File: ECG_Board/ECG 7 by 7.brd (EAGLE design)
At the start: 70 x 70 mm, 7 parts

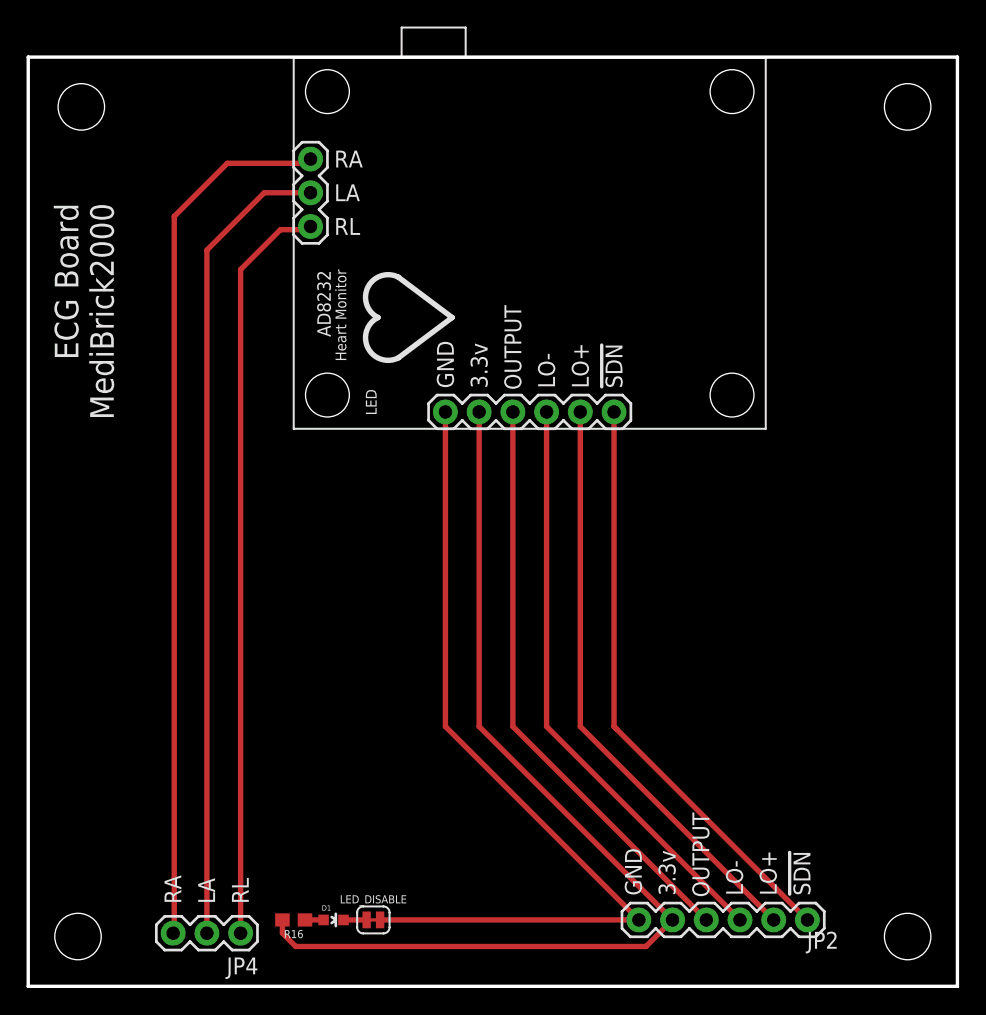
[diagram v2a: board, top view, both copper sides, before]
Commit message: Board Updates
Separated analog and digital ground
Updated routing
Updated silk labeling
Sound board with ES8388 included
Impedance and ECG board
Working on IMU board
Working on Environmental Airquality board
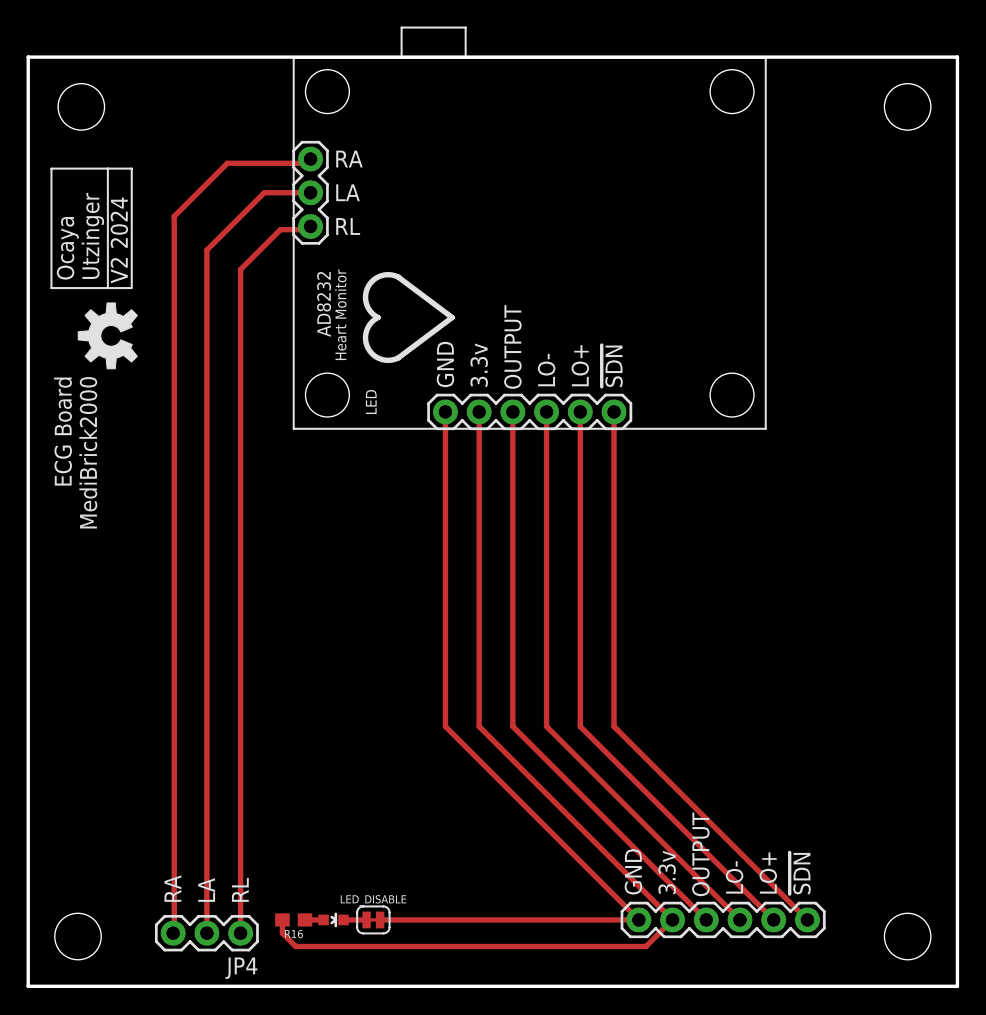
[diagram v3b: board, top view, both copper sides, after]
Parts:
- added U$2: (no value), SparkFun-Aesthetics:OSHW-LOGO-M
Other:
- board text added: "Ocaya Utzinger"
- board text added: "V2 2024"
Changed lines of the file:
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@@
 <text x="10.9" y="6.208" size="1.27" layer="21" font="vector" ratio="15" rot="R90" align="center-left">RA</text>
 <text x="15.98" y="6.208" size="1.27" layer="21" font="vector" ratio="15" rot="R90" align="center-left">RL</text>
-<text x="2" y="59" size="1.778" layer="25" rot="R270">ECG Board
+<text x="2" y="46" size="1.27" layer="25" rot="R270">ECG Board
 MediBrick2000</text>
 <dimension x1="30.5" y1="72" x2="0" y2="72" x3="15.25" y3="75" textsize="1.778" layer="1"/>
+<text x="5.35" y="53.15" size="1.27" layer="25" font="vector" ratio="20" rot="R90">Ocaya
+Utzinger</text>
+<wire x1="1.75" y1="52.6" x2="1.75" y2="61.6" width="0.1524" layer="25"/>
+<wire x1="1.75" y1="61.6" x2="6" y2="61.6" width="0.1524" layer="25"/>
+<wire x1="6" y1="61.6" x2="6" y2="52.6" width="0.1524" layer="25"/>
+<wire x1="6" y1="52.6" x2="1.75" y2="52.6" width="0.1524" layer="25"/>
+<wire x1="7.8" y1="52.65" x2="7.8" y2="61.6" width="0.1524" layer="25"/>
+<wire x1="7.8" y1="52.6" x2="6" y2="52.6" width="0.1524" layer="25"/>
+<wire x1="7.8" y1="61.6" x2="6" y2="61.6" width="0.1524" layer="25"/>
+<text x="7.5" y="52.95" size="1.27" layer="25" font="vector" ratio="20" rot="R90">V2 2024</text>
 </plain>
 <attributes>
@@
 <elements>
 <element name="JP2" library="SparkFun-Connectors" package="1X06" value="" x="46" y="5" smashed="yes">
-<attribute name="NAME" x="58.6538" y="2.8288" size="1.27" layer="25" ratio="10"/>
+<attribute name="NAME" x="58.6538" y="2.8288" size="1.27" layer="25" ratio="10" display="off"/>
 <attribute name="VALUE" x="44.73" y="1.825" size="1.27" layer="27"/>
 </element>
@@
 </element>
 <element name="D1" library="SparkFun-LED" package="LED-0603" value="RED" x="23" y="5" smashed="yes" rot="R270">
-<attribute name="NAME" x="22.111" y="5.6985" size="0.4064" layer="25"/>
+<attribute name="NAME" x="22.619" y="3.6665" size="0.6096" layer="27"/>
 <attribute name="PROD_ID" value="DIO-00819" x="28" y="12" size="1.778" layer="27" rot="R270" display="off"/>
-<attribute name="VALUE" x="21.984" y="3.9205" size="0.4064" layer="27"/>
+<attribute name="VALUE" x="21.984" y="3.9205" size="0.4064" layer="27" display="off"/>
 </element>
 <element name="LED_DISABLE" library="SparkFun-Jumpers" library_urn="urn:adsk.eagle:library:528" package="SMT-JUMPER_2_NC_TRACE_SILK" package3d_urn="urn:adsk.eagle:package:39281/1" value="JUMPER-SMT_2_NC_TRACE_SILK" x="26" y="5" smashed="yes" rot="R180">
 <attribute name="NAME" x="26" y="6.857" size="0.6096" layer="25" font="vector" ratio="20" rot="R180" align="bottom-center"/>
-<attribute name="VALUE" x="26" y="7.143" size="0.6096" layer="27" font="vector" ratio="20" rot="R180" align="top-center"/>
+<attribute name="VALUE" x="26" y="7.143" size="0.6096" layer="27" font="vector" ratio="20" rot="R180" align="top-center" display="off"/>
 </element>
 <element name="FRAME1" library="SparkFun-Aesthetics" library_urn="urn:adsk.eagle:library:507" package="DUMMY" package3d_urn="urn:adsk.eagle:package:37104/1" value="FRAME-LETTERNO_PACKAGE" x="-3" y="-1" smashed="yes">
@@
 </element>
 <element name="U$1" library="SPARK_ECG" package="SPARK_ECG" value="" x="20" y="42" smashed="yes"/>
+<element name="U$2" library="SparkFun-Aesthetics" library_urn="urn:adsk.eagle:library:507" package="OSHW-LOGO-M" package3d_urn="urn:adsk.eagle:package:37126/1" value="" x="6.25" y="49" smashed="yes" rot="R90"/>
 </elements>
 <signals>
